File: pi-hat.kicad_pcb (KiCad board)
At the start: 2 copper layers, 65 x 70.5 mm, 42 parts, among them J1 Raspberry_Pi_2_3, J2 Conn_SPI, J3 Conn_RTC, J4 Conn_01x08, J5 USB_B, J7 USB_OUT, J8 Jack-DC, M1 Motor_Servo, M2 Motor_Servo, M3 Motor_Servo, Q1 Q_NMOS_GDS, Q2 Q_NMOS_GDS, Q4 Q_NMOS_GDS, Q5 Q_NMOS_GDS, SW1 SW_Push, SW2 SW_Push, SW3 SW_DPST_x2, U1 ATTINY85-20SU

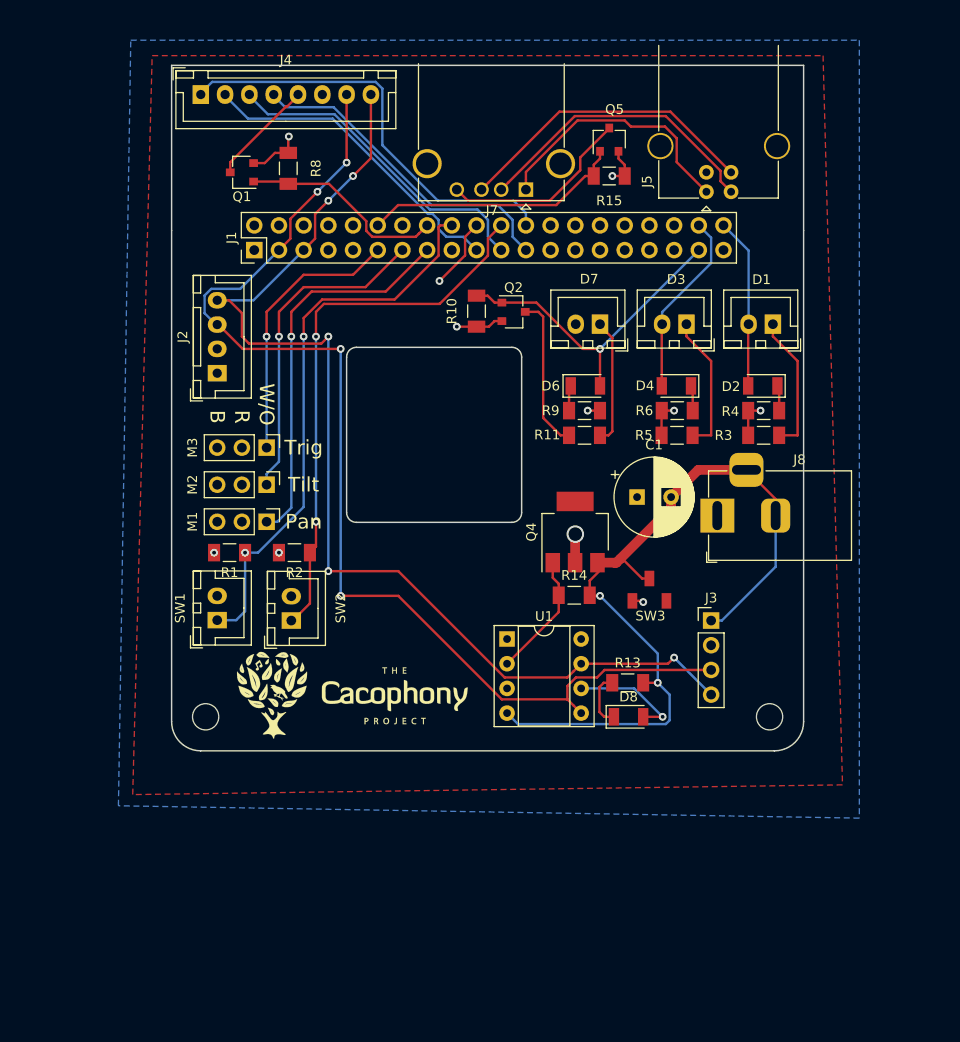
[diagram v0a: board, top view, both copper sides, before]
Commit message: updated pi hat to latest version.
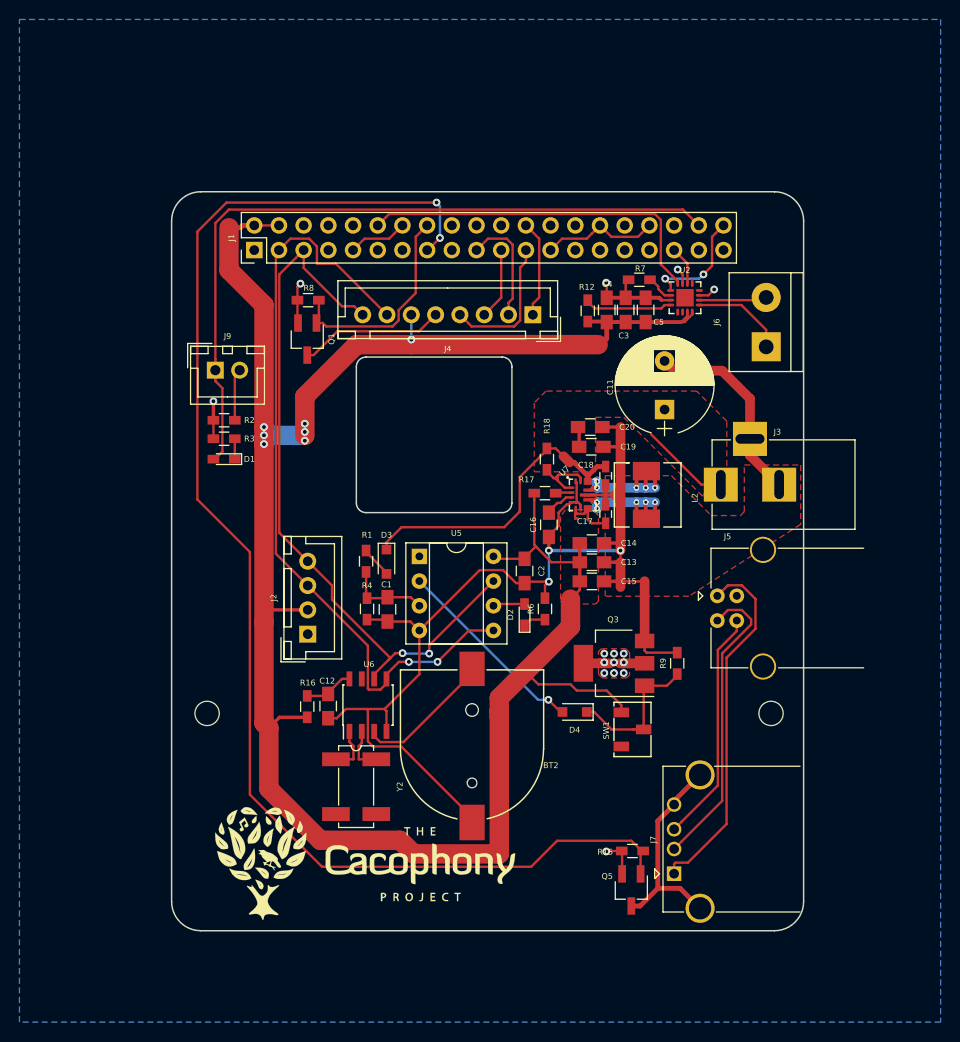
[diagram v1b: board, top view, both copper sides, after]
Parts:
- removed D6, D8: LED, LED_SMD:LED_1206_3216Metric_Pad1.07x1.80mm_HandSolder
- removed D7: LED, Connector_JST:JST_XH_B02B-XH-A_1x02_P2.50mm_Vertical
- removed the G*** at (118.7, 150.7)
- removed J8: Jack-DC, Connector_BarrelJack:BarrelJack_Horizontal
- removed M1, M2, M3: Motor_Servo, Connector_PinHeader_2.54mm:PinHeader_1x03_P2.54mm_Vertical
- removed MK1, MK2: Mounting_Hole, MountingHole:MountingHole_2.7mm_M2.5
- removed Q2: Q_NMOS_GDS, Package_TO_SOT_SMD:SC-59
- removed Q4: Q_NMOS_GDS, Package_TO_SOT_SMD:SOT-223
- removed R10, R14: 100K, Resistor_SMD:R_1206_3216Metric_Pad1.24x1.80mm_HandSolder
- removed R11: 100R, Resistor_SMD:R_1206_3216Metric_Pad1.24x1.80mm_HandSolder
- removed R13, R5: 470R, Resistor_SMD:R_1206_3216Metric_Pad1.24x1.80mm_HandSolder
- removed SW2: SW_Push, Connector_JST:JST_XH_B02B-XH-A_1x02_P2.50mm_Vertical
- removed SW3: SW_DPST_x2, switch-footprint:CJS-1200A1
- removed U1: ATTINY85-20SU, Package_DIP:DIP-8_W7.62mm_Socket
- added BT2: 1206, pi-hat-footprints:CR1220, F.Cu at (130.9, 156.3)
- added C11: 820uF, Capacitors_THT:CP_Radial_D10.0mm_P5.00mm, F.Cu at (150.7, 121.4)
- added C12: 10uF, Capacitors_SMD:C_0805_HandSoldering, F.Cu at (116.1, 151.9)
- added C13: 22uF, Capacitors_SMD:C_0805_HandSoldering, F.Cu at (143.2, 137.1)
- added C14: 22uF, Capacitors_SMD:C_0805_HandSoldering, F.Cu at (143.2, 135.1)
- added C15: 22uF, Capacitors_SMD:C_0805_HandSoldering, F.Cu at (143.2, 139.1)
- added C16: 100nF, Capacitors_SMD:C_0805_HandSoldering, F.Cu at (138.8, 133.2)
- added C17: 10uF, Capacitors_SMD:C_0603_HandSoldering, F.Cu at (144.6, 132.1)
- added C18: 10uF, Capacitors_SMD:C_0603_HandSoldering, F.Cu at (144.6, 128.2)
- added C19: 10uF, Capacitors_SMD:C_0805_HandSoldering, F.Cu at (143.2, 125.2)
- added C2: 1uF, Capacitors_SMD:C_0805_HandSoldering, F.Cu at (136.3, 138.0)
- added C20: 10uF, Capacitors_SMD:C_0805_HandSoldering, F.Cu at (143.1, 123.2)
- added C3: 10uF, Capacitors_SMD:C_0805_HandSoldering, F.Cu at (146.7, 111.1)
- added C4: 0.1uF, Capacitors_SMD:C_0805_HandSoldering, F.Cu at (144.8, 111.1)
- added C5: 10uF, Capacitors_SMD:C_0805_HandSoldering, F.Cu at (148.8, 111.2)
- added G***: LOGO, logo:logo6, F.Cu at (120.0, 168.0)
- added J6: Conn_01x02, Connectors:bornier2, F.Cu at (161.2, 115.0)
- added J9: Conn_01x02, Connectors_JST:JST_XH_B02B-XH-A_02x2.50mm_Straight, F.Cu at (104.5, 117.3)
- added L2: 1.5uH, pi-hat-footprints:ETQP3MxxxKVP, F.Cu at (148.8, 130.2)
- added Q3: Q_NMOS_GDS, TO_SOT_Packages_SMD:SOT-223, F.Cu at (145.5, 147.5)
- added R12: 634K, Resistors_SMD:R_0603_HandSoldering, F.Cu at (142.8, 111.2)
- added R16: 1K, Resistors_SMD:R_0603_HandSoldering, F.Cu at (114.0, 151.9)
- added R17: 100K, Resistors_SMD:R_0603_HandSoldering, F.Cu at (138.4, 130.0)
- added R18: 10k, Resistors_SMD:R_0603_HandSoldering, F.Cu at (138.6, 126.5)
- added R7: 100K, Resistors_SMD:R_0603_HandSoldering, F.Cu at (148.1, 108.0)
- added REF**: MountingHole_2.5mm, Mounting_Holes:MountingHole_2.5mm, F.Cu at (103.7, 152.7)
- added REF**: MountingHole_2.5mm, Mounting_Holes:MountingHole_2.5mm, F.Cu at (161.7, 152.7)
- added U2: MAX98357, Housings_DFN_QFN:QFN-16-1EP_3x3mm_Pitch0.5mm, F.Cu at (152.8, 109.9)
- added U5: ATTINY85-20SU, Housings_DIP:DIP-8_W7.62mm_Socket, F.Cu at (125.5, 136.5)
- added U6: PCF8523, Housings_SOIC:SOIC-8_3.9x4.9mm_Pitch1.27mm, F.Cu at (120.2, 151.8)
- added U7: TPS630701, pi-hat-footprints:TPS63070, F.Cu at (142.3, 130.2)
- added Y2: 32.768, Crystals:Crystal_SMD_SeikoEpson_MC306-4pin_8.0x3.2mm_HandSoldering, F.Cu at (119.0, 160.2)
- C1: value CP -> 1uF; footprint Capacitor_THT:CP_Radial_D8.0mm_P3.50mm -> Capacitors_SMD:C_0805_HandSoldering
- D1: footprint Connector_JST:JST_XH_B02B-XH-A_1x02_P2.50mm_Vertical -> LEDs:LED_0603_HandSoldering
- D2: value LED -> LED_GREEN; footprint LED_SMD:LED_1206_3216Metric_Pad1.07x1.80mm_HandSolder -> LEDs:LED_0603_HandSoldering
- D3: value LED -> D_Zener; footprint Connector_JST:JST_XH_B02B-XH-A_1x02_P2.50mm_Vertical -> Diodes_SMD:D_SOD-323_HandSoldering
- D4: value LED -> D; footprint LED_SMD:LED_1206_3216Metric_Pad1.07x1.80mm_HandSolder -> Diodes_SMD:D_SOD-323_HandSoldering
- J1: footprint Connector_PinHeader_2.54mm:PinHeader_2x20_P2.54mm_Vertical -> Pin_Headers:Pin_Header_Straight_2x20_Pitch2.54mm
- J2: footprint Connector_JST:JST_XH_B04B-XH-A_1x04_P2.50mm_Vertical -> Connectors_JST:JST_XH_B04B-XH-A_04x2.50mm_Straight
- J3: value Conn_RTC -> Jack-DC; footprint Connector_PinHeader_2.54mm:PinHeader_1x04_P2.54mm_Vertical -> Connectors:BARREL_JACK
- J4: footprint Connector_JST:JST_XH_B08B-XH-A_1x08_P2.50mm_Vertical -> Connectors_JST:JST_XH_B08B-XH-A_08x2.50mm_Straight
- Q1, Q5: footprint Package_TO_SOT_SMD:SC-59 -> TO_SOT_Packages_SMD:SC-59_Handsoldering
- R1: value 100K -> 1K; footprint Resistor_SMD:R_1206_3216Metric_Pad1.24x1.80mm_HandSolder -> Resistors_SMD:R_0603_HandSoldering
- R15, R3, R6, R8: footprint Resistor_SMD:R_1206_3216Metric_Pad1.24x1.80mm_HandSolder -> Resistors_SMD:R_0603_HandSoldering
- R2: value 100K -> 470R; footprint Resistor_SMD:R_1206_3216Metric_Pad1.24x1.80mm_HandSolder -> Resistors_SMD:R_0603_HandSoldering
- R4: value 470R -> 10K; footprint Resistor_SMD:R_1206_3216Metric_Pad1.24x1.80mm_HandSolder -> Resistors_SMD:R_0603_HandSoldering
- R9: value 470R -> 100K; footprint Resistor_SMD:R_1206_3216Metric_Pad1.24x1.80mm_HandSolder -> Resistors_SMD:R_0603_HandSoldering
- SW1: value SW_Push -> SW_DPST_x2; footprint Connector_JST:JST_XH_B02B-XH-A_1x02_P2.50mm_Vertical -> switch-footprint:CJS-1200A1
- moved Q5 77.2 mm to (147.3, 170.8), turned to 270 degrees
- moved J7 72.0 mm to (151.7, 169.1), turned to 90 degrees
- moved R15 69.5 mm to (147.4, 166.8), turned to 180 degrees
- moved D1 58.1 mm to (105.4, 126.5)
- moved R3 55.5 mm to (105.4, 124.4)
- moved R4 45.6 mm to (120.1, 141.9), turned to 270 degrees
- moved SW1 44.2 mm to (147.4, 154.3), turned to 270 degrees
- moved J5 41.6 mm to (156.1, 140.6), turned to 0 degrees
- moved J4 41.0 mm to (137.2, 111.7), turned to 180 degrees
- moved D3 39.4 mm to (122.1, 137.1), turned to 270 degrees
- moved D4 35.1 mm to (141.4, 152.5)
- moved D2 34.0 mm to (136.3, 142.5), turned to 90 degrees
- moved J2 28.4 mm to (114.0, 144.5)
- moved C1 28.1 mm to (122.2, 141.9), turned to 270 degrees
- moved R9 27.7 mm to (152.0, 147.5), turned to 90 degrees
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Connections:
- net CameraPower renamed /THERMAL_POWER
- net Net-(J1-Pad19) renamed /SPI_MOSI
- net Net-(J1-Pad21) renamed /SPI_MISO
- net Net-(J1-Pad23) renamed /SPI_SCLK
- net Net-(J1-Pad24) renamed /SPI_CEO
- C1 pad 1: +5V -> Net-(C1-Pad1)
- C1 pad 2: Net-(C1-Pad2) -> /Always_On/Ground
- D1 pad 2: LED1 -> /LED1
- D2 pad 2: LED1 -> Net-(D2-Pad2)
- D3 pad 1: Net-(D3-Pad1) -> VCC
- D3 pad 2: LED2 -> Net-(D3-Pad2)
- D4 pad 2: LED2 -> Net-(D4-Pad2)
- J1 pad 11: ServoTrigger -> Net-(J1-Pad11)
- J1 pad 12: USBPower -> /I2S_BCLK
- J1 pad 13: ServoTilt -> Net-(J1-Pad13)
- J1 pad 15: ServoPan -> /USB_POWER
- J1 pad 18: Button1 -> Net-(J1-Pad18)
- J1 pad 22: Button2 -> Net-(J1-Pad22)
- J1 pad 3: SDA -> /SDA
- J1 pad 35: Net-(J1-Pad35) -> /I2S_LRCLK
- J1 pad 37: Laser -> Net-(J1-Pad37)
- J1 pad 38: LED2 -> /LED1
- J1 pad 40: LED1 -> /I2S_DIN
- J1 pad 5: SCL -> /SCL
- J2 pad 3: SDA -> /SDA
- J2 pad 4: SCL -> /SCL
- J3 pad 1: Net-(C1-Pad2) -> VCC
- J3 pad 2: +5V -> /Always_On/Ground
- J3 pad 3: SDA -> /Always_On/Ground
- J4 pad 7: SDA -> /SDA
- J4 pad 8: SCL -> /SCL
- J5 pad 5: Net-(J5-Pad5) -> GND
- J7 pad 5: Net-(J7-Pad5) -> Net-(J7-Pad4)
- Q5 pad 1: USBPower -> /USB_POWER
- R1 pad 1: Button1 -> Net-(D3-Pad2)
- R1 pad 2: GND -> Net-(C1-Pad1)
- R15 pad 1: USBPower -> /USB_POWER
- R2 pad 1: Button2 -> Net-(J9-Pad2)
- R4 pad 1: Net-(D2-Pad1) -> Net-(C1-Pad1)
- R4 pad 2: GND -> /Always_On/Ground
- R6 pad 1: Net-(D4-Pad1) -> Net-(D2-Pad1)
- R6 pad 2: GND -> /Always_On/Ground
- R9 pad 1: Net-(D6-Pad1) -> Net-(D4-Pad1)
- R9 pad 2: GND -> /Always_On/Ground
- SW1 pad 1: Button1 -> +5V
- SW1 pad 2: +5V -> Net-(D4-Pad1)
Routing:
- net +5V: track 0.00 -> 231.7 mm, vias 0 -> 7
- net /Always_On/Ground: track 0.00 -> 147.0 mm, vias 0 -> 3
- net /USB_POWER: track 0.00 -> 139.1 mm, vias 0 -> 2
- net SDA: track 117.8 -> 0.00 mm, vias 4 -> 0
- net SCL: track 115.3 -> 0.00 mm, vias 5 -> 0
- net Net-(C1-Pad2): track 82.5 -> 0.00 mm, vias 2 -> 0
- net /SDA: track 0.00 -> 81.0 mm, vias 0 -> 2
- net /LED1: track 0.00 -> 76.0 mm
- net /SCL: track 0.00 -> 74.9 mm, vias 0 -> 2
- net Button1: track 57.6 -> 0.00 mm, vias 2 -> 0
- net Button2: track 56.6 -> 0.00 mm, vias 2 -> 0
- net VCC: track 0.00 -> 43.3 mm
- net ServoPan: track 39.9 -> 0.00 mm, vias 1 -> 0
- net /I2S_BCLK: track 0.00 -> 37.1 mm
- net /SPI_CEO: track 44.3 -> 10.0 mm
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- added copper zone on F.Cu, net /Always_On/Ground
- added copper zone on F.Cu, net GND
- added copper zone on F.Cu, net VCC
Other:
- board size 65 x 70.5 mm -> 65 x 76 mm
- net class Default: clearance 0.2 -> 0.1
- rule trace_clearance: 0.2 -> 0.1
- board text removed: "B"
- board text removed: "Pan"
- board text removed: "R"
- board text removed: "Tilt"
- board text removed: "Trig"
- board text removed: "W/O"

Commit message: Updated to version 0.3
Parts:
- removed BT2: 1206, pi-hat-footprints:CR1220
- removed C12: 10uF, Capacitors_SMD:C_0805_HandSoldering
- removed D3: D_Zener, Diodes_SMD:D_SOD-323_HandSoldering
- removed D4: D, Diodes_SMD:D_SOD-323_HandSoldering
- removed the G*** at (120.0, 168.0)
- removed J9: Conn_01x02, Connectors_JST:JST_XH_B02B-XH-A_02x2.50mm_Straight
- removed R16: 1K, Resistors_SMD:R_0603_HandSoldering
- removed REF** (x2): MountingHole_2.5mm, Mounting_Holes:MountingHole_2.5mm
- removed SW1: SW_DPST_x2, switch-footprint:CJS-1200A1
- removed U6: PCF8523, Housings_SOIC:SOIC-8_3.9x4.9mm_Pitch1.27mm
- removed Y2: 32.768, Crystals:Crystal_SMD_SeikoEpson_MC306-4pin_8.0x3.2mm_HandSoldering
- added BT1: 1206, pi-hat-footprints:CR1220, F.Cu at (108.5, 163.1)
- added C6: 2.2uF, Capacitors_SMD:C_0603, F.Cu at (124.3, 150.9)
- added C7: 2.2uF, Capacitors_SMD:C_0603, F.Cu at (119.5, 126.2)
- added C8: 2.2uF, Capacitors_SMD:C_0603, F.Cu at (116.9, 128.2)
- added C9: 2.2uF, Capacitors_SMD:C_0603, F.Cu at (112.9, 126.2)
- added F1: Fuse, Resistors_SMD:R_0603_HandSoldering, F.Cu at (151.6, 129.3)
- added G***: LOGO, pi-hat-footprints:logo, F.Cu at (131.5, 163.8)
- added J8: Conn_01x04, Connectors_JST:JST_XH_B04B-XH-A_04x2.50mm_Straight, F.Cu at (130.9, 141.3)
- added MK1: Mounting_Hole, Mounting_Holes:MountingHole_3mm_Pad, F.Cu at (103.7, 152.7)
- added MK2: Mounting_Hole, Mounting_Holes:MountingHole_3mm_Pad, F.Cu at (161.7, 152.7)
- added Q2: Q_NMOS_GSD, TO_SOT_Packages_SMD:SOT-23, F.Cu at (125.6, 147.5)
- added R10: 100K, Resistors_SMD:R_0603, F.Cu at (123.4, 120.7)
- added R5: 470R, Resistors_SMD:R_0603, F.Cu at (126.7, 137.1)
- added U1: MAX485E, Housings_SSOP:MSOP-8_3x3mm_Pitch0.65mm, F.Cu at (122.6, 153.7)
- added U3: AP2210N-3.3TRG1, TO_SOT_Packages_SMD:SOT-23, F.Cu at (119.6, 129.0)
- added U4: ATTINY85-20SU, Housings_DIP:DIP-8_W7.62mm_Socket, F.Cu at (120.0, 123.3)
- added Y1: 32.768, Crystals:Crystal_SMD_SeikoEpson_MC306-4pin_8.0x3.2mm, F.Cu at (111.2, 141.6)
- C1: value 1uF -> 2.2uF; footprint Capacitors_SMD:C_0805_HandSoldering -> Capacitors_SMD:C_0603
- C13, C14, C15, C16, C19, C20, C3, C5: footprint Capacitors_SMD:C_0805_HandSoldering -> Capacitors_SMD:C_0805
- C17, C18: footprint Capacitors_SMD:C_0603_HandSoldering -> Capacitors_SMD:C_0603
- C2: value 1uF -> 10uF; footprint Capacitors_SMD:C_0805_HandSoldering -> Capacitors_SMD:C_0805
- C4: value 0.1uF -> 100nF; footprint Capacitors_SMD:C_0805_HandSoldering -> Capacitors_SMD:C_0805
- D1: value LED -> D_Zener; footprint LEDs:LED_0603_HandSoldering -> Diodes_SMD:D_SOD-323
- D2: value LED_GREEN -> LED_RED; footprint LEDs:LED_0603_HandSoldering -> LEDs:LED_0603
- J2: value Conn_SPI -> Conn_01x04
- Q1, Q5: value Q_NMOS_GDS -> Q_NMOS_GSD; footprint TO_SOT_Packages_SMD:SC-59_Handsoldering -> TO_SOT_Packages_SMD:SOT-23
- Q3: value Q_NMOS_GDS -> Q_PMOS_DGS; footprint TO_SOT_Packages_SMD:SOT-223 -> digikey-footprints:IRF9310PbF
- R1, R12, R15, R17, R4, R6, R7, R8: footprint Resistors_SMD:R_0603_HandSoldering -> Resistors_SMD:R_0603
- R18: value 10k -> 10K; footprint Resistors_SMD:R_0603_HandSoldering -> Resistors_SMD:R_0603
- R2: value 470R -> 120R; footprint Resistors_SMD:R_0603_HandSoldering -> Resistors_SMD:R_0603
- R3: value 470R -> 100K; footprint Resistors_SMD:R_0603_HandSoldering -> Resistors_SMD:R_0603
- R9: value 100K -> 1K; footprint Resistors_SMD:R_0603_HandSoldering -> Resistors_SMD:R_0603
- U5: value ATTINY85-20SU -> PCF8523; footprint Housings_DIP:DIP-8_W7.62mm_Socket -> Housings_SOIC:SOIC-8_3.9x4.9mm_Pitch1.27mm
- moved R2 38.0 mm to (127.1, 153.7), turned to 270 degrees
- moved R9 32.7 mm to (121.7, 135.3), turned to 270 degrees
- moved R3 28.7 mm to (122.5, 147.5), turned to 270 degrees
- moved R18 23.2 mm to (139.5, 149.7)
- moved R17 22.5 mm to (138.8, 152.4)
- moved C18 21.9 mm to (145.8, 150.1)
- moved C19 21.9 mm to (144.4, 147.1)
- moved C20 21.9 mm to (144.2, 145.1)
- moved C16 21.9 mm to (140.0, 155.1)
- moved C17 21.9 mm to (145.8, 154.0)
- moved L2 21.9 mm to (150.0, 152.0)
- moved U7 21.9 mm to (143.5, 152.0)
- moved C13 21.6 mm to (144.4, 158.7)
- moved C14 21.6 mm to (144.4, 156.7)
- moved C15 21.6 mm to (144.4, 160.7)
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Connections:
- C1 pad 1: Net-(C1-Pad1) -> /Battery_Sense
- C1 pad 2: /Always_On/Ground -> GND
- C11 pad 2: /Always_On/Ground -> GND
- C13 pad 2: /Always_On/Ground -> GND
- C14 pad 2: /Always_On/Ground -> GND
- C15 pad 2: /Always_On/Ground -> GND
- C16 pad 2: /Always_On/Ground -> GND
- C17 pad 2: /Always_On/Ground -> GND
- C18 pad 2: /Always_On/Ground -> GND
- C19 pad 2: /Always_On/Ground -> GND
- C2 pad 1: +5V -> Net-(C2-Pad1)
- C2 pad 2: /Always_On/Ground -> GND
- C20 pad 2: /Always_On/Ground -> GND
- D1 pad 1: Net-(D1-Pad1) -> VCC
- D1 pad 2: /LED1 -> Net-(D1-Pad2)
- D2 pad 1: Net-(D2-Pad1) -> GND
- J1 pad 1: Net-(J1-Pad1) -> /RPi_3V3
- J1 pad 10: Net-(J1-Pad10) -> /Rx
- J1 pad 11: Net-(J1-Pad11) -> /Tx_enable
- J1 pad 17: Net-(J1-Pad17) -> /RPi_3V3
- J1 pad 38: /LED1 -> Net-(J1-Pad38)
- J1 pad 8: Net-(J1-Pad8) -> /Tx
- J2 pad 1: GND -> Net-(J2-Pad1)
- J2 pad 2: +5V -> Net-(J2-Pad2)
- J2 pad 3: /SDA -> VCC
- J2 pad 4: /SCL -> Net-(J2-Pad4)
- J3 pad 1: VCC -> Net-(F1-Pad2)
- J3 pad 2: /Always_On/Ground -> GND
- J3 pad 3: /Always_On/Ground -> GND
- J4 pad 6: +5V -> /RPi_3V3
- Q3 pad 1: Net-(D4-Pad1) -> Net-(F1-Pad1)
- Q3 pad 3: /Always_On/Ground -> VCC
- R1 pad 1: Net-(D3-Pad2) -> Net-(D1-Pad2)
- R1 pad 2: Net-(C1-Pad1) -> /Battery_Sense
- R2 pad 1: Net-(J9-Pad2) -> Net-(J2-Pad2)
- R2 pad 2: GND -> Net-(J2-Pad1)
- R3 pad 1: Net-(D1-Pad1) -> /Enable_trap
- R4 pad 1: Net-(C1-Pad1) -> /Battery_Sense
- R4 pad 2: /Always_On/Ground -> GND
- R6 pad 1: Net-(D2-Pad1) -> /LED_Indicator
- R6 pad 2: /Always_On/Ground -> Net-(D2-Pad2)
- R9 pad 1: Net-(D4-Pad1) -> +3V3
- R9 pad 2: /Always_On/Ground -> Net-(C2-Pad1)
- U5 pad 3: Net-(C1-Pad1) -> Net-(BT1-Pad1)
- U5 pad 4: /Always_On/Ground -> GND
- U5 pad 6: Net-(D2-Pad2) -> /SCL
- U5 pad 7: /SCL -> Net-(U5-Pad7)
- U5 pad 8: +5V -> Net-(C2-Pad1)
- U7 pad 10: /Always_On/Ground -> GND
- U7 pad 14: Net-(R18-Pad2) -> /5V_Enable
- U7 pad 15: /Always_On/Ground -> GND
- U7 pad 4: /Always_On/Ground -> GND
- U7 pad 6: /Always_On/Ground -> GND
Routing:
- net /Always_On/Ground: track 147.0 -> 0.00 mm, vias 3 -> 0
- net /Tx_enable: track 0.00 -> 88.1 mm, vias 0 -> 2
- net /Rx: track 0.00 -> 81.6 mm, vias 0 -> 2
- net /LED1: track 76.0 -> 0.00 mm
- net /Tx: track 0.00 -> 62.2 mm
- net /5V_Enable: track 0.00 -> 50.0 mm, vias 0 -> 2
- net GND: track 49.3 -> 97.8 mm, vias 15 -> 18
- net +5V: track 231.7 -> 190.1 mm, vias 7 -> 2
- net Net-(BT1-Pad1): track 0.00 -> 37.0 mm, vias 0 -> 2
- net /LED_Indicator: track 0.00 -> 28.1 mm, vias 0 -> 2
- net VCC: track 43.3 -> 66.0 mm
- net /Battery_Sense: track 0.00 -> 19.2 mm
- net +3V3: track 0.00 -> 19.1 mm, vias 0 -> 1
- net /SPI_CEO: track 10.0 -> 29.0 mm
- net Net-(U5-Pad2): track 20.3 -> 2.77 mm, vias 1 -> 0
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- added copper zone on F.Cu, net (none)
- added copper zone on F.Cu, net Net-(F1-Pad1)
- added copper zone on F.Cu, net Net-(F1-Pad2)
- removed copper zone on F.Cu, net /Always_On/Ground
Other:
- board size 65 x 76 mm -> 65 x 74.5 mm
- board text added: "Camera"
- board text added: "Reset"
- board text added: "Trap"
- board text added: "V0.3"

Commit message: Version 4
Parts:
- added FID1: FIDUCIAL, Fiducials:Fiducial_1mm_Dia_2.54mm_Outer_CopperTop, F.Cu at (163.0, 170.2)
- added FID2: FIDUCIAL, Fiducials:Fiducial_1mm_Dia_2.54mm_Outer_CopperTop, F.Cu at (117.8, 170.2)
- added FID3: FIDUCIAL, Fiducials:Fiducial_1mm_Dia_2.54mm_Outer_CopperTop, F.Cu at (163.0, 107.5)
- BT1: value 1206 -> 1220
- C11: value 820uF -> 270uF; footprint Capacitors_THT:CP_Radial_D10.0mm_P5.00mm -> Capacitors_THT:CP_Radial_D8.0mm_P3.50mm
- J6: footprint Connectors:bornier2 -> Connectors_JST:JST_XH_B02B-XH-A_02x2.50mm_Straight
- J8: footprint Connectors_JST:JST_XH_B04B-XH-A_04x2.50mm_Straight -> Connectors_JST:JST_PH_B4B-PH-K_04x2.00mm_Straight
- moved F1 13.4 mm to (142.8, 139.4), turned to 90 degrees
- moved C11 11.7 mm to (143.0, 127.0), turned to 270 degrees
- moved Q3 10.0 mm to (152.5, 126.2), turned to 270 degrees
- moved J8 1.05 mm to (130.9, 140.2)
- moved J6 0.68 mm to (160.5, 114.8), turned to 270 degrees
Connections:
- C11 pad 1: VCC -> Net-(C11-Pad1)
- F1 pad 1: Net-(F1-Pad1) -> VCC
- F1 pad 2: Net-(F1-Pad2) -> Net-(C11-Pad1)
- J1 pad 13: Net-(J1-Pad13) -> /Enable_trap
- J3 pad 1: Net-(F1-Pad2) -> Net-(J3-Pad1)
- Q3 pad 1: Net-(F1-Pad1) -> Net-(J3-Pad1)
- Q3 pad 3: VCC -> Net-(C11-Pad1)
- U1 pad 1: /Tx -> /Rx
- U1 pad 4: /Rx -> /Tx
- U2 pad 10: Net-(J6-Pad2) -> Net-(J6-Pad1)
- U2 pad 9: Net-(J6-Pad1) -> Net-(J6-Pad2)
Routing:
- net /Enable_trap: track 1.87 -> 49.0 mm, vias 0 -> 6
- net GND: track 97.8 -> 87.1 mm
- net Net-(J6-Pad2): track 6.99 -> 11.2 mm
- net /5V_Enable: track 50.0 -> 46.9 mm
- net /Rx: track 81.6 -> 83.8 mm
- net /Tx: track 62.2 -> 63.6 mm
- net Net-(J6-Pad1): track 9.68 -> 8.91 mm
- net (no net): vias 1 -> 0
- added copper zone on F.Cu, net Net-(C11-Pad1)
- added copper zone on F.Cu, net Net-(J3-Pad1)
- removed copper zone on F.Cu, net Net-(F1-Pad1)
- removed copper zone on F.Cu, net Net-(F1-Pad2)
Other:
- board text added: "Speaker"
- board text added: "V0.4"
- board text removed: "V0.3"
